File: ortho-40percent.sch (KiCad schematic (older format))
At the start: 28 parts, among them J1 USB-C_Receptacle-24, SW1 SW_NO_4-Pin, U1 U_TPD4E05U06DQAR, U2 U_ATmega32u4-MU, Y1 XTAL_4Lead

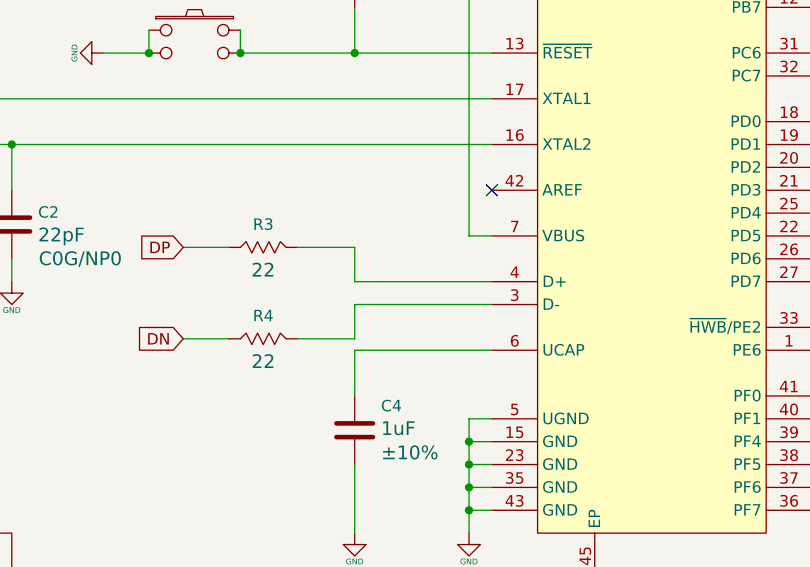
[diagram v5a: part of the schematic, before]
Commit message: USB connector update
Added connector keepout zone and PCB edge text for usb-c connector footprint. Attempted routing and movement of D+/D- lines.
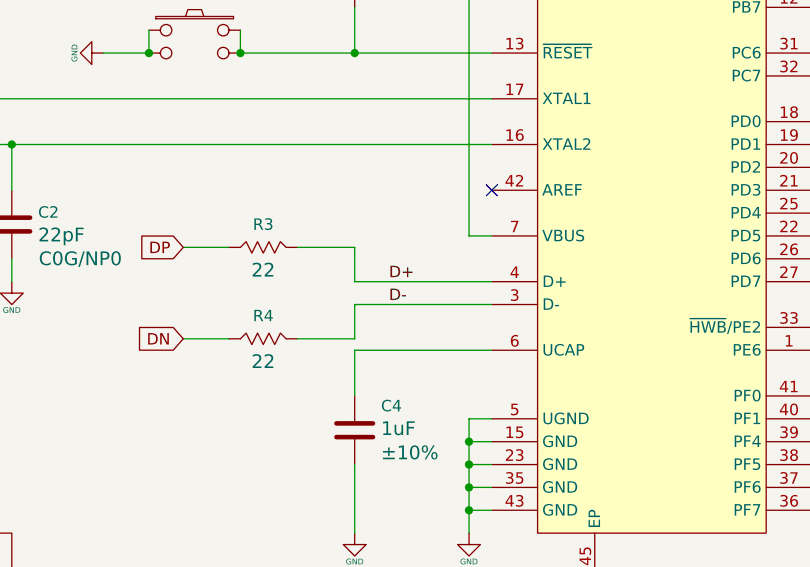
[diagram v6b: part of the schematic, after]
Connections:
- net D-: now reaches R4.1, U2.3 (D-)
- net D+: now reaches R3.1, U2.4 (D+)
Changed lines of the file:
@@
 Wire Wire Line
 	9050 5250 9050 5200
+Text Label 8150 3900 0    50   ~ 0
+D+
+Text Label 8150 4000 0    50   ~ 0
+D-
 $EndSCHEMATC

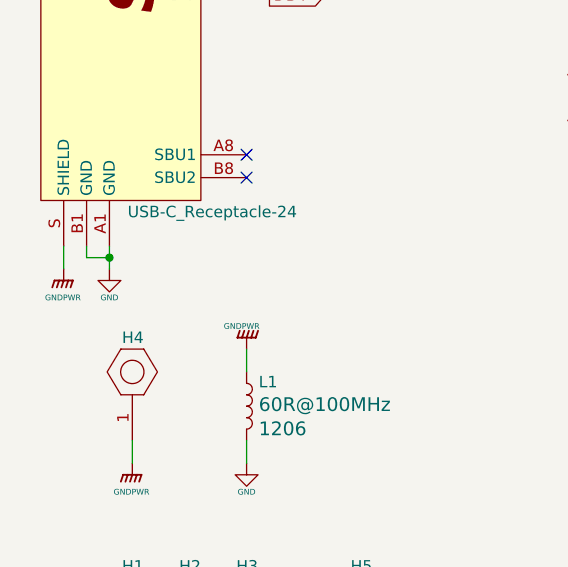
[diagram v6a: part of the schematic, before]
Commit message: Beginning switch routing
Finished routing of all micro, usb, and power components. Beginning placement and routing of diodes and keyswitches.
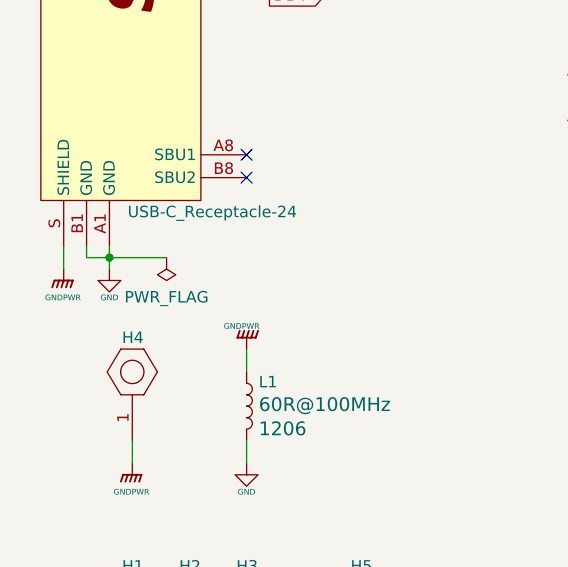
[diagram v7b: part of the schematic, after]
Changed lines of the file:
@@
 Text Label 8150 4000 0    50   ~ 0
 D-
+$Comp
+L power:PWR_FLAG #FLG?
+U 1 1 6090B270
+P 1650 3600
+F 0 "#FLG?" H 1650 3675 50  0001 C CNN
+F 1 "PWR_FLAG" H 1650 3773 50  0000 C CNN
+F 2 "" H 1650 3600 50  0001 C CNN
+F 3 "~" H 1650 3600 50  0001 C CNN
+	1    1650 3600
+	-1   0    0    1
+$EndComp
+Wire Wire Line
+	1650 3600 1400 3600
 $EndSCHEMATC
